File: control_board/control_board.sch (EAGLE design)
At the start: 65 parts, among them IC1 ATMEGA1284P-MU, J1 USB Female Type C Connector, J5 20021311-00010T4LF, J6 20021311-00010T4LF, J7 20021311-00010T4LF, Q2 BSS84-7-F, Q3 BSS138PW,115, SW1 SPST_TACT-KMR2, U1 915MHz, U3 MCP73833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

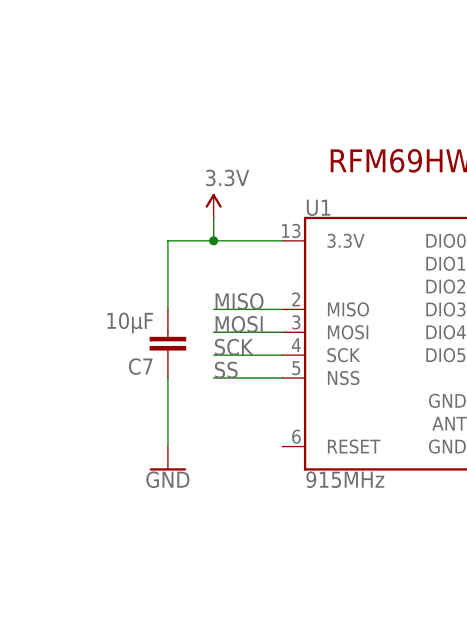
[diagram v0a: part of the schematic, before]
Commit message: Added pullup on SS pin of radio
- Without pullup, bootloader can't be loaded
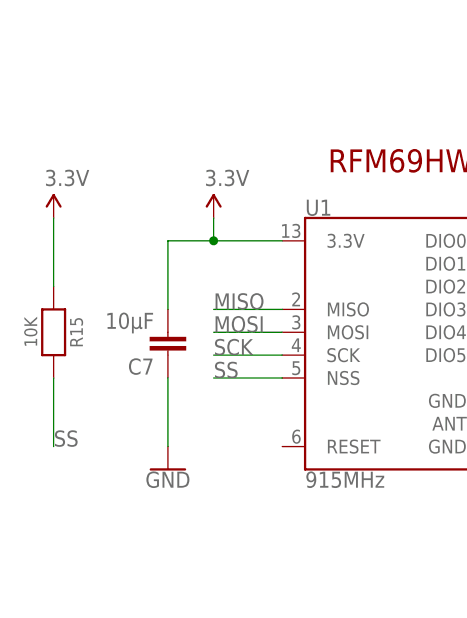
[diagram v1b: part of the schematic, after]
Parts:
- added R15: 10K, Adafruit Feather 32u4 Bluefruit LE:MICROBUILDER_RESISTOR_0402MP
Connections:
- net SS: now also R15.2
- net VCC: now also R15.1
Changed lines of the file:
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@@
 <part name="C1" library="SparkFun-Capacitors" deviceset="0.33UF/330NF" device="-0805-50V-10%" override_package3d_urn="urn:adsk.eagle:package:24879823/2" override_package_urn="urn:adsk.eagle:footprint:24879824/1" value="10µF"/>
 <part name="C7" library="SparkFun-Capacitors" deviceset="0.33UF/330NF" device="-0805-50V-10%" override_package3d_urn="urn:adsk.eagle:package:24879912/2" override_package_urn="urn:adsk.eagle:footprint:24879913/1" value="10µF"/>
+<part name="R15" library="Adafruit Feather 32u4 Bluefruit LE" deviceset="MICROBUILDER_RESISTOR" device="_0402MP" override_package3d_urn="urn:adsk.eagle:package:24877243/2" override_package_urn="urn:adsk.eagle:footprint:24877244/1" value="10K">
+<attribute name="MPN" value="RC0402FR-7W10KL"/>
+</part>
+<part name="P+7" library="SparkFun" deviceset="VCC" device="" value="3.3V"/>
 </parts>
 <sheets>
@@
 <attribute name="NAME" x="-39.624" y="9.779" size="1.778" layer="95" font="vector" rot="R180"/>
 <attribute name="VALUE" x="-39.624" y="14.859" size="1.778" layer="96" font="vector" rot="R180"/>
+</instance>
+<instance part="R15" gate="G$1" x="-50.8" y="12.7" smashed="yes" rot="R270">
+<attribute name="MPN" x="-50.8" y="12.7" size="1.778" layer="96" rot="R270" display="off"/>
+<attribute name="NAME" x="-48.26" y="12.7" size="1.4224" layer="95" rot="R270" align="center"/>
+<attribute name="VALUE" x="-53.34" y="12.7" size="1.4224" layer="96" ratio="15" rot="R270" align="center"/>
+</instance>
+<instance part="P+7" gate="1" x="-50.8" y="25.4" smashed="yes">
+<attribute name="VALUE" x="-51.816" y="28.956" size="1.778" layer="96"/>
 </instance>
 </instances>
@@
 </segment>
 <segment>
+<pinref part="GND10" gate="1" pin="GND"/>
 <wire x1="-38.1" y1="7.62" x2="-38.1" y2="0" width="0.1524" layer="91"/>
-<pinref part="GND10" gate="1" pin="GND"/>
 <pinref part="C7" gate="G$1" pin="1"/>
 </segment>
@@
 <junction x="210.82" y="10.16"/>
 </segment>
+<segment>
+<pinref part="P+7" gate="1" pin="VCC"/>
+<pinref part="R15" gate="G$1" pin="1"/>
+<wire x1="-50.8" y1="25.4" x2="-50.8" y2="17.78" width="0.1524" layer="91"/>
+</segment>
 </net>
 <net name="VIN" class="1">
@@
 <label x="-33.02" y="7.62" size="1.778" layer="95"/>
 </segment>
-</net>
+<segment>
+<pinref part="R15" gate="G$1" pin="2"/>
+<wire x1="-50.8" y1="7.62" x2="-50.8" y2="0" width="0.1524" layer="91"/>
+<label x="-50.8" y="0" size="1.778" layer="95"/>
+</segment>
+</net>

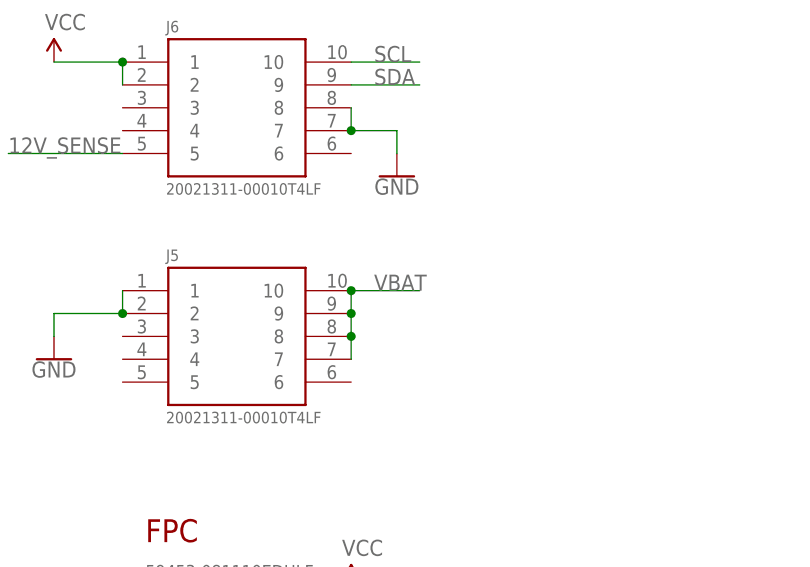
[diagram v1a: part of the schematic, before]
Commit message: v0.3 - fixed VIN power
- Changed VBAT to VIN on headers so the power board works even when there is no battery present
- Changed resistor dividor traces so it connects to proper VBAT circuit
- small trace and silkscreen modifications
- updated gerbers
- ERC/DRC
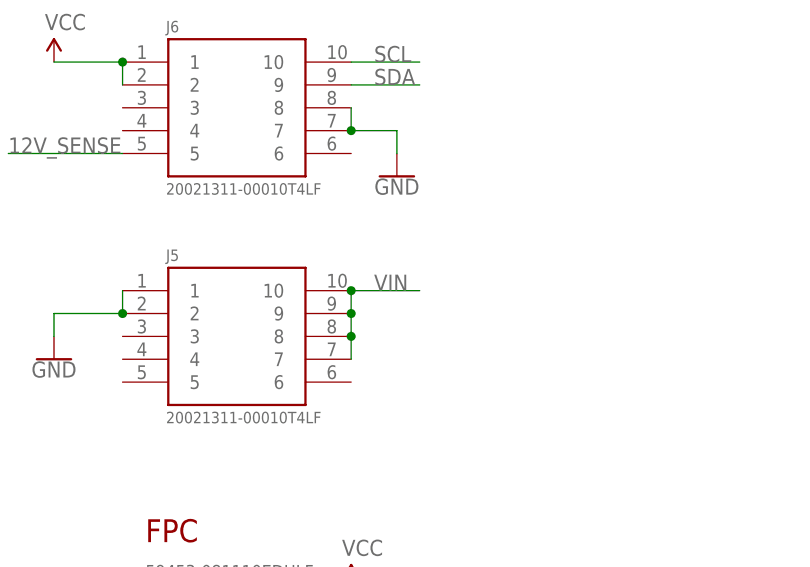
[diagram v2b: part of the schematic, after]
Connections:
- net VBAT: no longer J5.10, J5.7, J5.8, J5.9
- net VIN: now also J5.10, J5.7, J5.8, J5.9

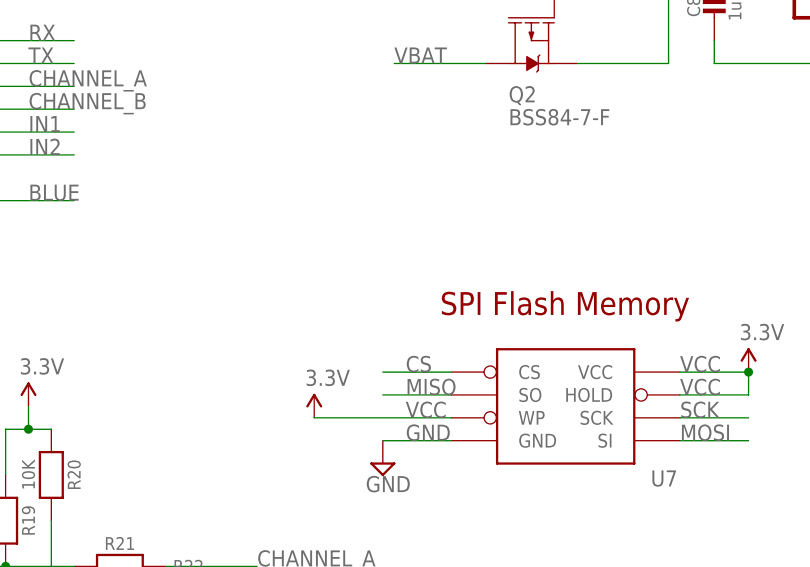
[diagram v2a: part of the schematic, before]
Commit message: v0.4 - added pullup on flash SS
- flash SS now has pullup to allow bootload while flash is installed
- updated gerbers only
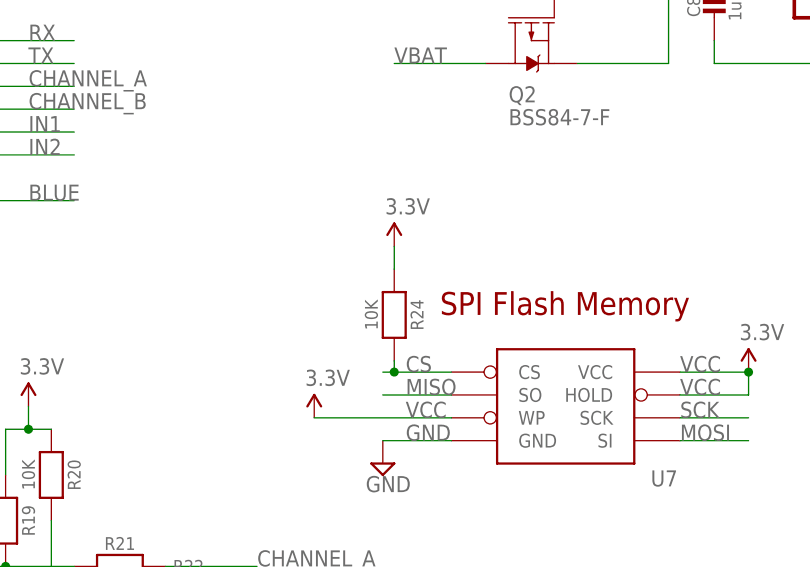
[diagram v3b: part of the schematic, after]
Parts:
- added R24: 10K, Adafruit Feather 32u4 Bluefruit LE:MICROBUILDER_RESISTOR_0402MP
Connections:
- net CS: now also R24.2
- net VCC: now also R24.1
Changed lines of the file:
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@@
 </part>
 <part name="P+7" library="SparkFun" deviceset="VCC" device="" value="3.3V"/>
+<part name="R24" library="Adafruit Feather 32u4 Bluefruit LE" deviceset="MICROBUILDER_RESISTOR" device="_0402MP" override_package3d_urn="urn:adsk.eagle:package:24877243/2" override_package_urn="urn:adsk.eagle:footprint:24877244/1" value="10K">
+<attribute name="MPN" value="RC0402FR-7W10KL"/>
+</part>
+<part name="P+8" library="SparkFun" deviceset="VCC" device="" value="3.3V"/>
 </parts>
 <sheets>
@@
 <instance part="P+7" gate="1" x="-50.8" y="25.4" smashed="yes">
 <attribute name="VALUE" x="-51.816" y="28.956" size="1.778" layer="96"/>
+</instance>
+<instance part="R24" gate="G$1" x="137.16" y="27.94" smashed="yes" rot="R270">
+<attribute name="MPN" x="137.16" y="27.94" size="1.778" layer="96" rot="R270" display="off"/>
+<attribute name="NAME" x="139.7" y="27.94" size="1.4224" layer="95" rot="R270" align="center"/>
+<attribute name="VALUE" x="134.62" y="27.94" size="1.4224" layer="96" ratio="15" rot="R270" align="center"/>
+</instance>
+<instance part="P+8" gate="1" x="137.16" y="35.56" smashed="yes">
+<attribute name="VALUE" x="136.144" y="39.116" size="1.778" layer="96"/>
 </instance>
 </instances>
@@
 <wire x1="-50.8" y1="25.4" x2="-50.8" y2="17.78" width="0.1524" layer="91"/>
 </segment>
+<segment>
+<pinref part="R24" gate="G$1" pin="1"/>
+<pinref part="P+8" gate="1" pin="VCC"/>
+<wire x1="137.16" y1="33.02" x2="137.16" y2="35.56" width="0.1524" layer="91"/>
+</segment>
 </net>
 <net name="VIN" class="1">
@@
 <net name="CS" class="0">
 <segment>
-<wire x1="143.51" y1="21.59" x2="135.89" y2="21.59" width="0.1524" layer="91"/>
+<wire x1="143.51" y1="21.59" x2="137.16" y2="21.59" width="0.1524" layer="91"/>
 <label x="138.43" y="21.59" size="1.778" layer="95"/>
 <pinref part="U7" gate="G$1" pin="CS"/>
-</segment>
-<segment>
+<pinref part="R24" gate="G$1" pin="2"/>
+<wire x1="137.16" y1="21.59" x2="135.89" y2="21.59" width="0.1524" layer="91"/>
+<wire x1="137.16" y1="22.86" x2="137.16" y2="21.59" width="0.1524" layer="91"/>
+<junction x="137.16" y="21.59"/>
+</segment>
+<segment>

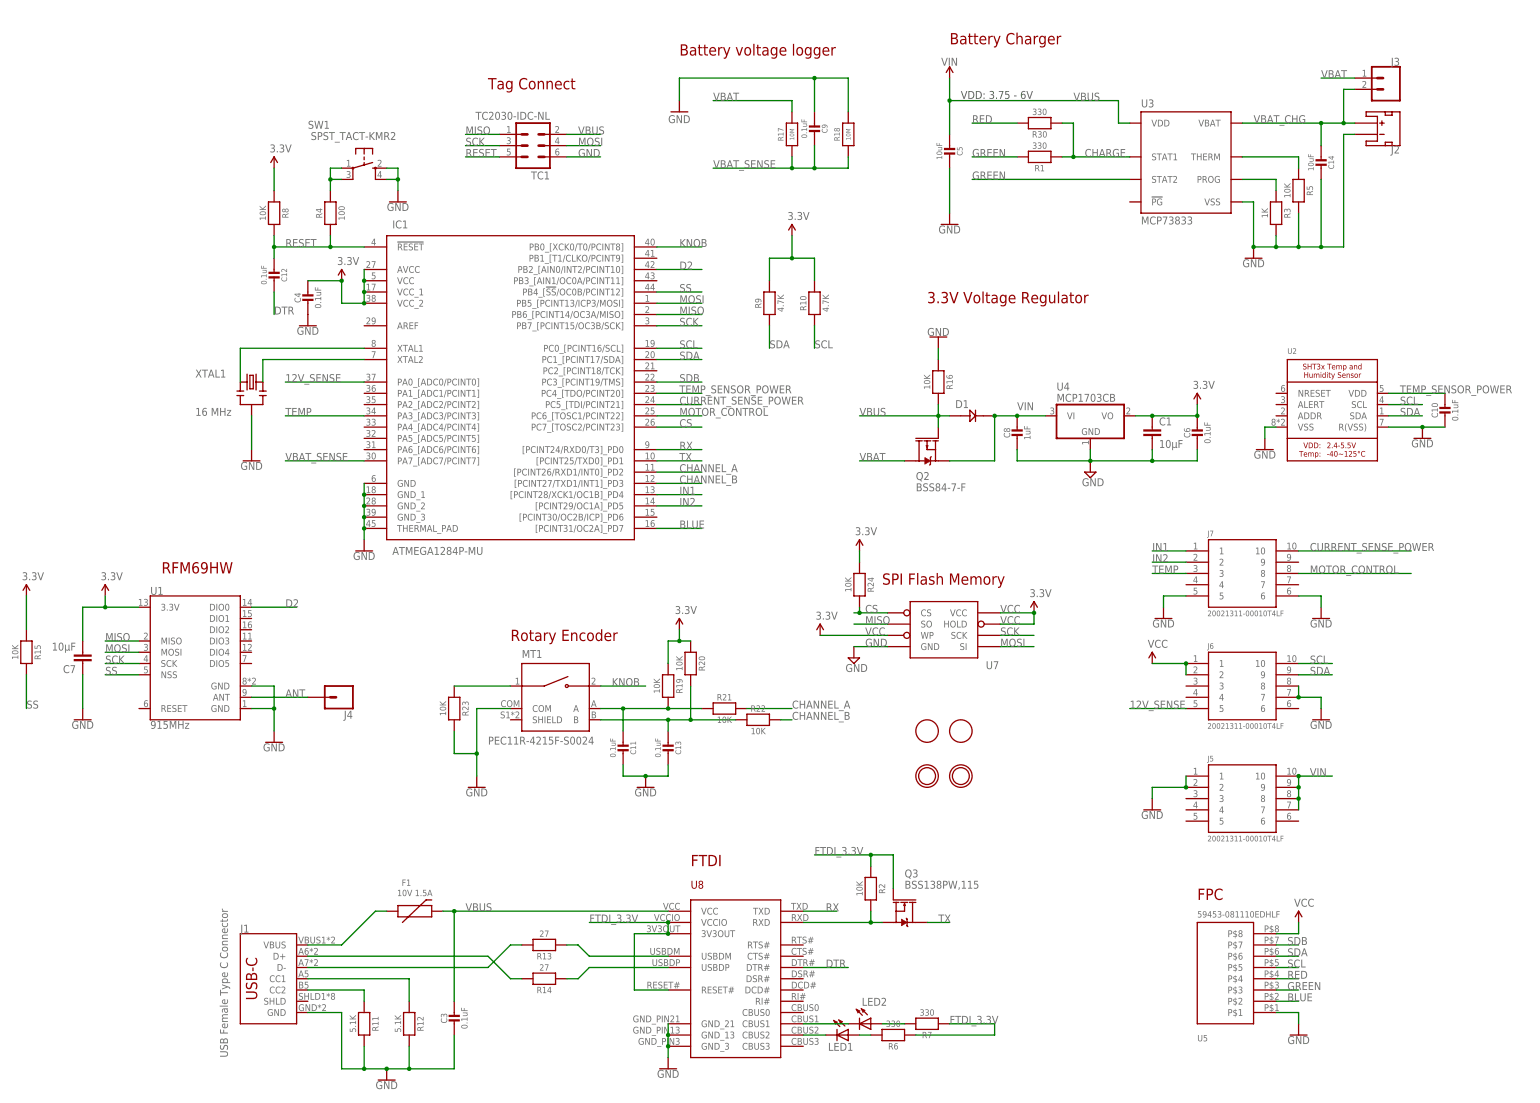
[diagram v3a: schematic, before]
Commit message: v0.5 - major revision
- Replaced charger with smaller one (lower current consumption)
- Added power and charge LEDs
- wired red, green and blue LEDs
- replaced 12V sense with VBUS sense (current sensor monitors voltage as well)
- minor trace fixes
- updated gerbers and renders
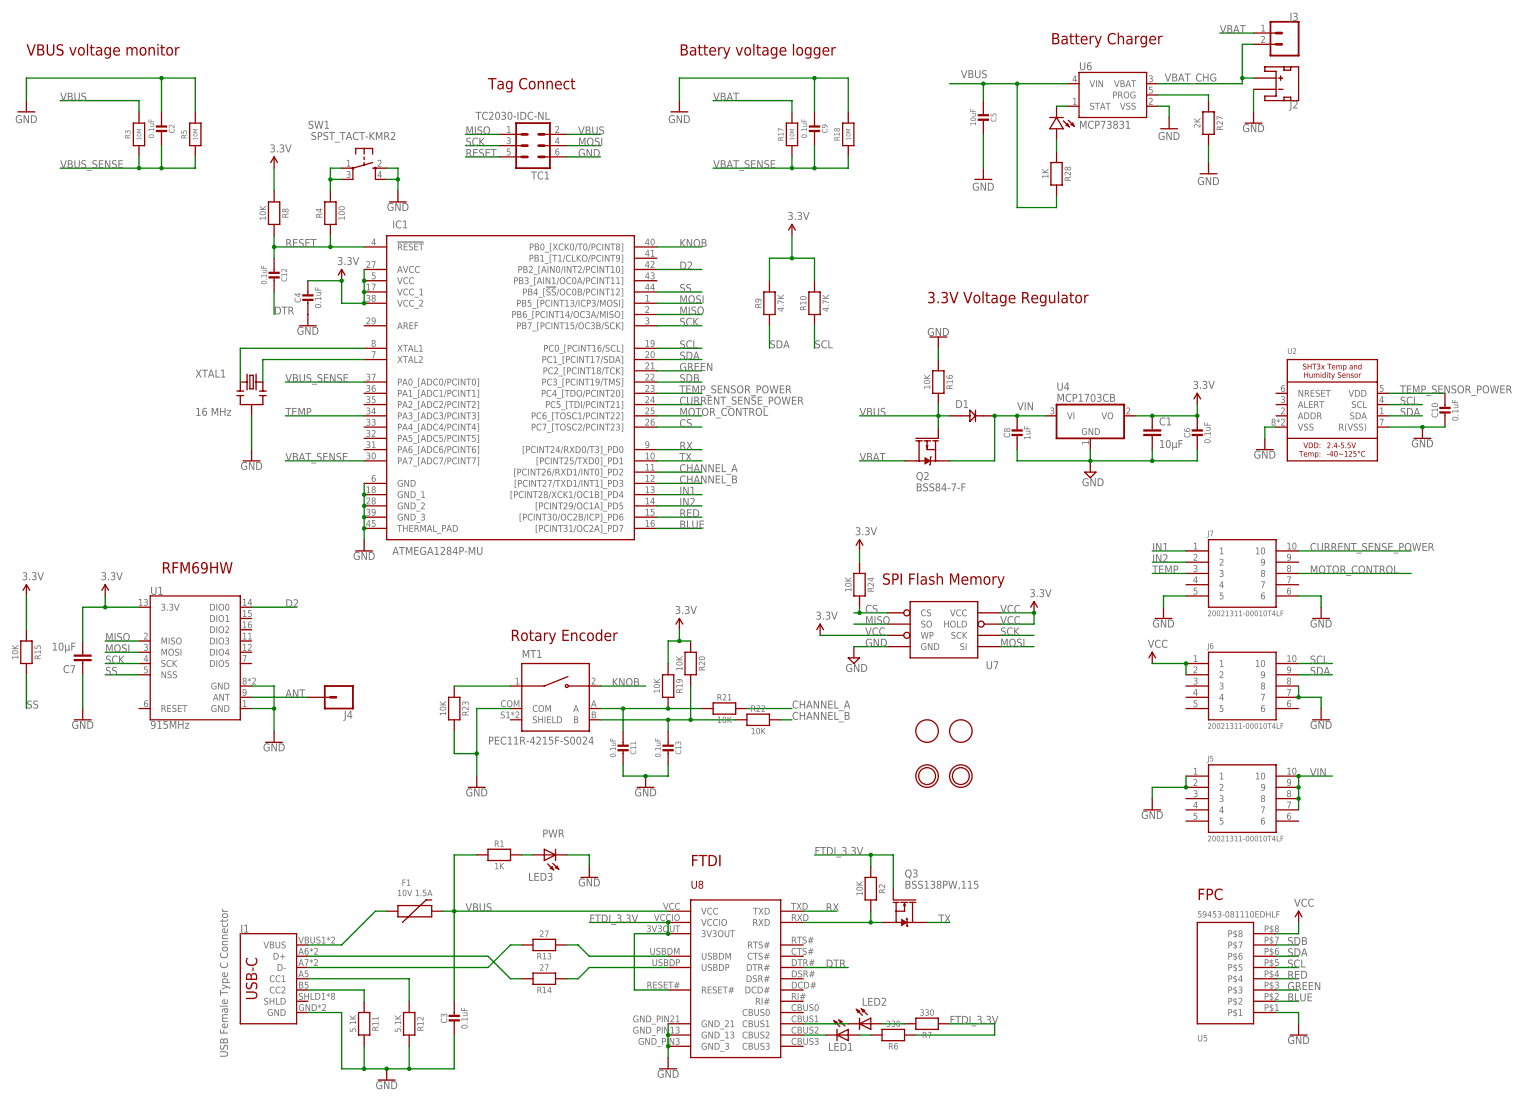
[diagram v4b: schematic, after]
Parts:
- removed C14: 10uF, Adafruit Feather 32u4 Bluefruit LE:MICROBUILDER_CAP_CERAMIC_0402MP
- removed R30: 330, Adafruit Feather 32u4 Bluefruit LE:MICROBUILDER_RESISTOR_0402MP
- removed U3: MCP73833, SparkFun-IC-Power:MCP73833
- added C2: 0.1uF, Adafruit Feather 32u4 Bluefruit LE:MICROBUILDER_CAP_CERAMIC_0402MP
- added LED3: PWR, adafruit:LEDCHIPLED_0603
- added LED4: LED0603, LowPowerLab:LED0603
- added R27: 2K, Adafruit Feather 32u4 Bluefruit LE:MICROBUILDER_RESISTOR_0402MP
- added R28: 1K, Adafruit Feather 32u4 Bluefruit LE:MICROBUILDER_RESISTOR_0402MP
- added U6: MCP73831, SparkFun:MCP73831
- R1: value 330 -> 1K
- R3: value 1K -> 10M; MPN RC0402FR-7W10KL -> RC0402JR-0710KL
- R5: value 10K -> 10M; MPN RC0402FR-7W10KL -> RC0402JR-0710KL
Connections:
- removed net 12V_SENSE: IC1.PA0_[ADC0/PCINT0], J6.5
- removed net CHARGE: R1.1, R30.1, U3.STAT1
- removed net PROG: R3.1, U3.PROG
- removed net THERM: R5.1, U3.THERM
- new net N$16: LED4.PLUS, R28.1
- new net N$19: LED4.MINUS, U6.STAT
- new net N$2: LED3.A, R1.2
- new net PROG1: R27.1, U6.PROG
- new net VBUS_SENSE: C2.1, IC1.PA0_[ADC0/PCINT0], R3.1, R5.1
- net GND: now also C2.2, LED3.C, R27.2, U6.VSS; no longer C14.1, R3.2, U3.VSS
- net GREEN: now also IC1.PC2_[PCINT18/TCK]; no longer R1.2, U3.STAT2
- net RED: now also IC1.[PCINT30/OC2B/ICP]_PD6; no longer R30.2
- net VBAT_CHG: now also U6.VBAT; no longer C14.2, U3.VBAT
- net VBUS: now also R1.1, R28.2, R3.2, U6.VIN; no longer U3.VDD
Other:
- note added: "VBUS voltage monitor"
- note removed: "VDD: 3.75 - 6V"
- moved on the sheet: C5, J2, J3, R1, R3, R5

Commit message: v0.6 - control board design update
- changed green pin to a PWM pin
- Added driver power control pin
- updated gerbers, render, schematic
- ERC/DRC
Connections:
- new net DRIVER_POWER: IC1.PC2_[PCINT18/TCK], J6.5
- net GREEN: now also IC1.PB3_[AIN1/OC0A/PCINT11]; no longer IC1.PC2_[PCINT18/TCK]
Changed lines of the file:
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@@
 </segment>
 <segment>
-<pinref part="IC1" gate="G$1" pin="PC2_[PCINT18/TCK]"/>
-<wire x1="91.44" y1="76.2" x2="101.6" y2="76.2" width="0.1524" layer="91"/>
-<label x="96.52" y="76.2" size="1.778" layer="95"/>
+<pinref part="IC1" gate="G$1" pin="PB3_[AIN1/OC0A/PCINT11]"/>
+<wire x1="91.44" y1="96.52" x2="101.6" y2="96.52" width="0.1524" layer="91"/>
+<label x="96.52" y="96.52" size="1.778" layer="95"/>
 </segment>
 </net>
@@
 </segment>
 </net>
+<net name="DRIVER_POWER" class="0">
+<segment>
+<pinref part="IC1" gate="G$1" pin="PC2_[PCINT18/TCK]"/>
+<wire x1="91.44" y1="76.2" x2="101.6" y2="76.2" width="0.1524" layer="91"/>
+<label x="96.52" y="76.2" size="1.778" layer="95"/>
+</segment>
+<segment>
+<pinref part="J6" gate="G$1" pin="5"/>
+<wire x1="210.82" y1="0" x2="203.2" y2="0" width="0.1524" layer="91"/>
+<label x="190.5" y="0" size="1.778" layer="95"/>
+</segment>
+</net>
